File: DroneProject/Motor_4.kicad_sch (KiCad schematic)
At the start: 0 parts

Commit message: Finished motor and C1 designs, still need to rename components on MTR2, 3, and 4 pages
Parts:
- added C40, C56: 1uF, Capacitor_SMD:C_0402_1005Metric, symbol Device:C
- added C50: 10uF, Capacitor_SMD:C_1206_3216Metric, symbol Device:C
- added C55, C73, C76: 0.1uF, Capacitor_SMD:C_0402_1005Metric, symbol Device:C
- added C57: 47nF, Capacitor_SMD:C_0402_1005Metric, symbol Device:C
- added C58, C59: 270uF, Capacitor_SMD:CP_Elec_10x10.5, symbol Device:C_Polarized
- added C60, C70, C71, C72, C74, C75: 1uF, Capacitor_SMD:C_0603_1608Metric, symbol Device:C
- added NT10, NT11, NT12, NT9: NetTie_2, NetTie:NetTie-2_SMD_Pad0.5mm, symbol Device:NetTie_2
- added Q13, Q14, Q15, Q16, Q17, Q18: CSD17577Q5A, Package_TO_SOT_SMD:TDSON-8-1, symbol Transistor_FET:CSD17577Q5A
- added R13, R14, R15: 10K, Resistor_SMD:R_0402_1005Metric, symbol Device:R_US
- added R16: 33, Resistor_SMD:R_0402_1005Metric, symbol Device:R_US
- added R17, R18: CSS2H-2512K-2L00J, Resistor_SMD:R_2512_6332Metric, symbol Device:R
- added U7: DRV8320SRTVR, Library:DRV8320SRTVR, symbol Global:DRV8320SRTVR
- added U8, U9: INA180A2, Package_TO_SOT_SMD:SOT-23-5, symbol Amplifier_Current:INA180A2
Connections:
- new net: C57.1, U7.32 (CPL)
- new net: C57.2, U7.1 (CPH)
- new net: NT10.2, U8.4 (-)
- new net: Q17.4 (G), U7.13 (GHC)
- new net: NT11.1, Q16.1 (S), Q16.2 (S), Q16.3 (S), R18.1, U7.9 (SLB)
- new net: Q16.4 (G), U7.10 (GLB)
- new net: NT9.1, Q14.1 (S), Q14.2 (S), Q14.3 (S), R17.1, U7.8 (SLA)
- new net: NT9.2, U8.3 (+)
- new net: NT11.2, U9.3 (+)
- new net: Q13.4 (G), U7.5 (GHA)
- new net: C56.2, U7.2 (VCP)
- new net: Q15.4 (G), U7.12 (GHB)
- new net: Q18.4 (G), U7.15 (GLC)
- new net: R16.2, U7.18 (SDO)
- new net: Q14.4 (G), U7.7 (GLA)
- new net: NT12.2, U9.4 (-)
- new net +3.3V: C73.1, C76.1, R13.2, R14.2, R15.2, U8.5 (V+), U9.5 (V+)
- new net C1_SPI2_MISO: R16.1
- new net C1_SPI2_MOSI: U7.19 (SDI)
- new net C1_SPI2_SCK: U7.20 (SCK)
- new net GND: C40.2, C73.2, C76.2, U7.23 (AGND), U7.33 (PAD), U8.2 (GND), U9.2 (GND)
- new net GNDPWR: C50.2, C55.2, C58.2, C59.2, C60.2, C70.2, C71.2, C72.2, C74.2, C75.2, NT10.1, NT12.1, Q18.1 (S), Q18.2 (S), Q18.3 (S), R17.2, R18.2, U7.16 (SLC), U7.31 (PGND)
- new net MTR1_DVDD: C40.1, U7.24 (DVDD)
- new net MTR4_A: Q13.1 (S), Q13.2 (S), Q13.3 (S), Q14.5 (D), U7.6 (SHA)
- new net MTR4_A_PWM: U7.25 (INHA)
- new net MTR4_B: Q15.1 (S), Q15.2 (S), Q15.3 (S), Q16.5 (D), U7.11 (SHB)
- new net MTR4_B_PWM: U7.27 (INHB)
- new net MTR4_C: Q17.1 (S), Q17.2 (S), Q17.3 (S), Q18.5 (D), U7.14 (SHC)
- new net MTR4_CSN: R15.1, U7.21 (nSCS)
- new net MTR4_CURR_A: U8.1
- new net MTR4_CURR_B: U9.1
- new net MTR4_C_PWM: U7.29 (INHC)
- new net MTR4_EN: R14.1, U7.22 (ENABLE)
- new net MTR4_FAULT_N: R13.1, U7.17 (FAULT_N)
- new net VDD: C50.1, C55.1, C56.1, C58.1, C59.1, C60.1, C70.1, C71.1, C72.1, C74.1, C75.1, Q13.5 (D), Q15.5 (D), Q17.5 (D), U7.3 (VM), U7.4 (VDRAIN)

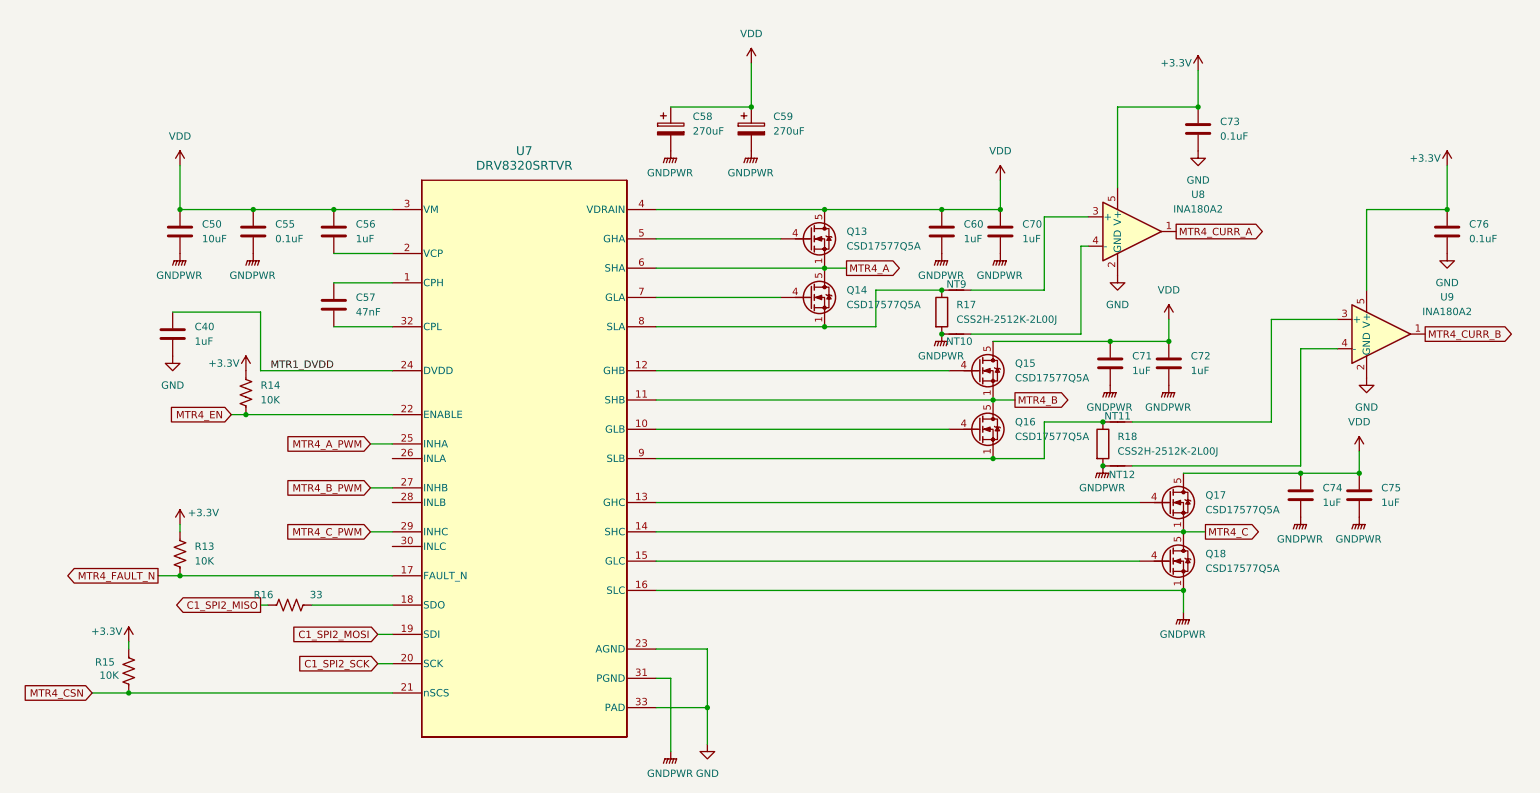
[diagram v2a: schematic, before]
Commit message: Finished most of routing for motor controls, however likely going to revert back and make separate ESC boards for motor control as I think that would honestly be more efficient from both a cost and debug complexity standpoint.
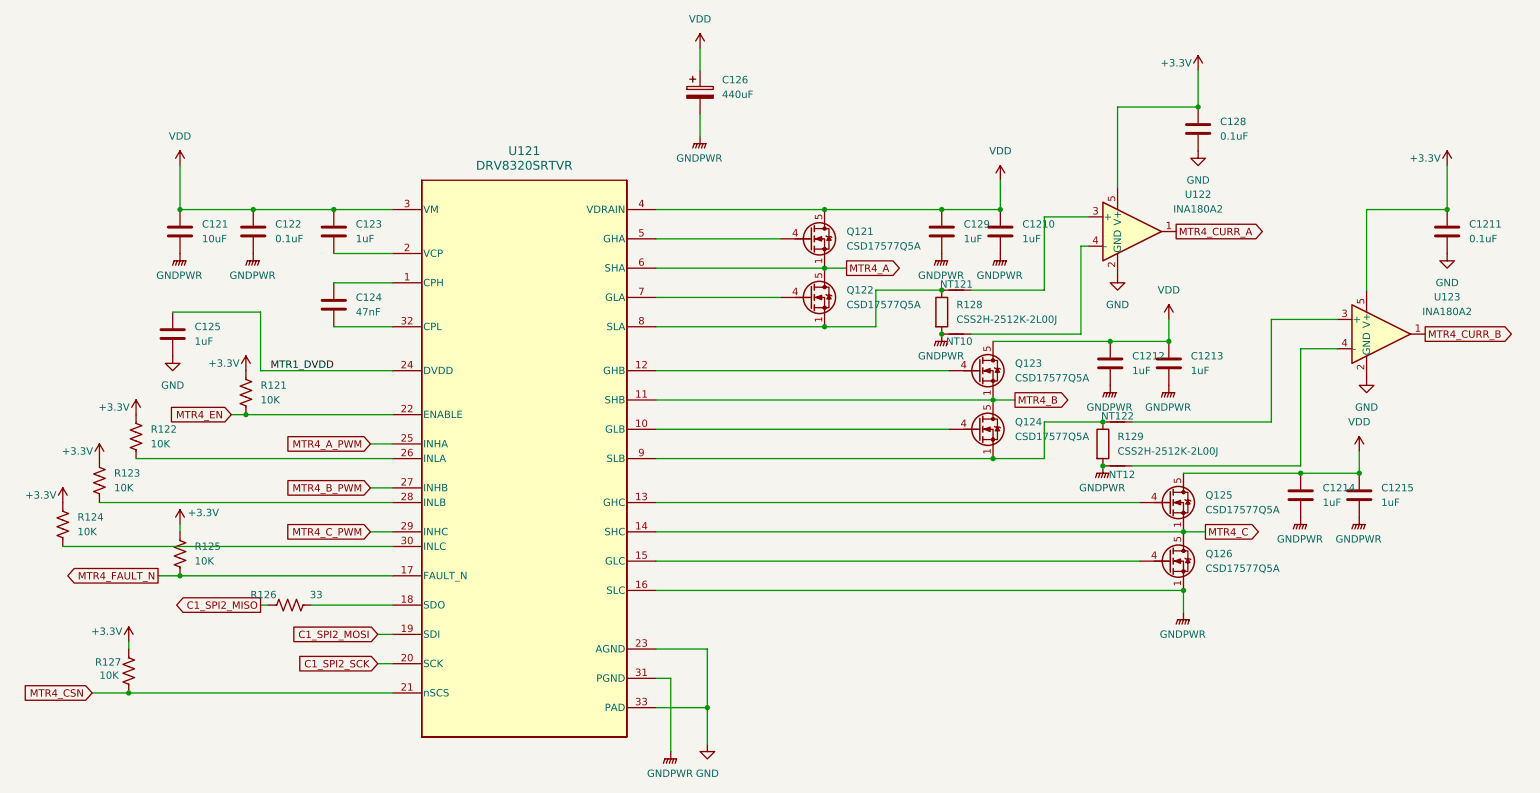
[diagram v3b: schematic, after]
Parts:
- removed C58, C59: 270uF, Capacitor_SMD:CP_Elec_10x10.5, symbol Device:C_Polarized
- added C126: 440uF, Capacitor_THT:CP_Radial_D10.0mm_P5.00mm, symbol Device:C_Polarized
- added R122, R123, R124: 10K, Resistor_SMD:R_0402_1005Metric, symbol Device:R_US
- renumbered C50 to C121, C70 to C1210, C76 to C1211, C71 to C1212, C72 to C1213, C74 to C1214, C75 to C1215, C55 to C122, C56 to C123, C57 to C124, C40 to C125, C73 to C128, C60 to C129, NT9 to NT121, NT11 to NT122, Q13 to Q121, Q14 to Q122, Q15 to Q123, Q16 to Q124, Q17 to Q125, Q18 to Q126, R14 to R121, R13 to R125, R16 to R126, R15 to R127, R17 to R128, R18 to R129, U7 to U121, U8 to U122, U9 to U123
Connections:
- net +3.3V: now also R122.2, R123.2, R124.2
- net GNDPWR: now also C126.2
- net VDD: now also C126.1
- net at U121.26 (INLA): now also R122.1
- net at U121.28 (INLB): now also R123.1
- net at U121.30 (INLC): now also R124.1
